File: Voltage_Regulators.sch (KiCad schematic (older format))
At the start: 28 parts, among them Q5 RTQ020N03, U1 LM2675_Adj, U2 LM2675_5V, U5 TLV2371_DBV

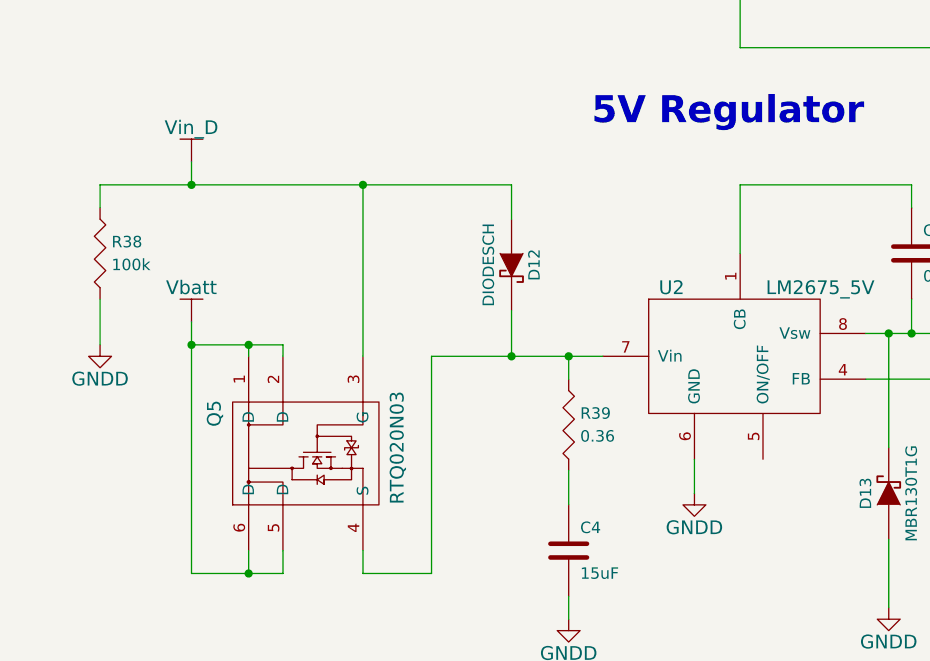
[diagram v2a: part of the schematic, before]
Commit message: Cleared all DRC errors.
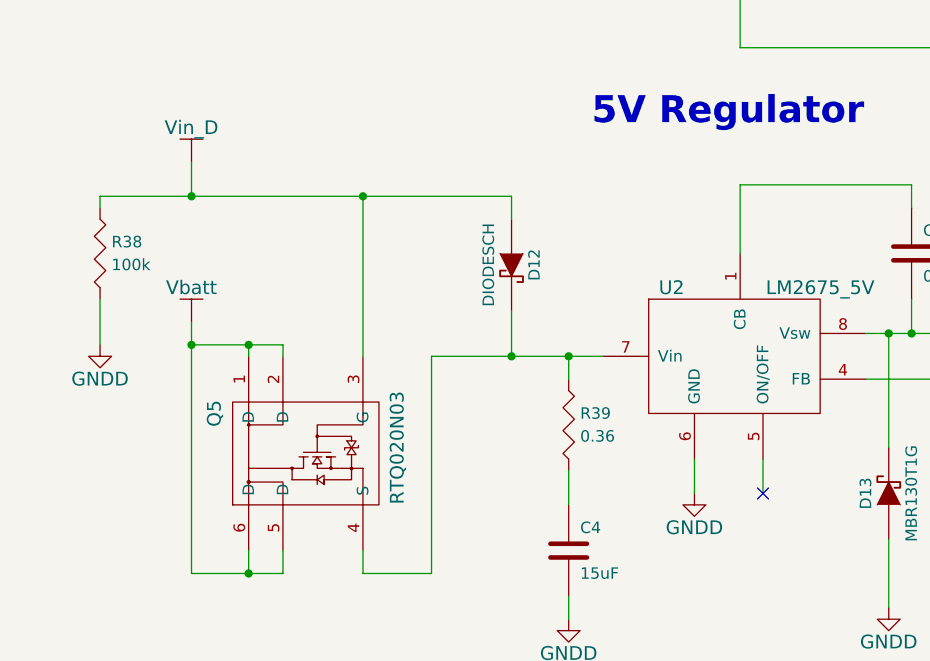
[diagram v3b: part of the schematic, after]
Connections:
- no-connect marks 0 -> 1
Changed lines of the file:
@@
 	5150 4900 5150 4700
 Connection ~ 5150 4900
-Wire Wire Line
-	5150 4150 5150 4300
-Wire Wire Line
-	3350 4150 5150 4150
-Wire Wire Line
-	4500 4150 4500 4900
-Connection ~ 4500 4150
-Wire Wire Line
-	3750 4150 3750 4050
 $Comp
 L Vbatt #PWR025
@@
 Wire Wire Line
 	3350 4650 3350 4850
-Wire Wire Line
-	3350 4250 3350 4150
-Connection ~ 3750 4150
 Text Notes 7600 1000 0    118  ~ 24
 8V Regulator
@@
 	1    0    0    -1
 $EndComp
+Wire Wire Line
+	4800 4900 4800 5850
+Wire Wire Line
+	4800 5850 4500 5850
+Wire Wire Line
+	4500 5850 4500 5750
+Wire Wire Line
+	4150 5850 4150 5750
+Wire Wire Line
+	3750 5850 4150 5850
+Wire Wire Line
+	4000 5850 4000 5750
+Connection ~ 4000 5850
+Wire Wire Line
+	3750 4850 4150 4850
+Wire Wire Line
+	4150 4850 4150 4900
+Connection ~ 3750 4850
+Wire Wire Line
+	4000 4850 4000 4900
+Connection ~ 4000 4850
+$Comp
+L TLV2371_DBV U5
+U 1 1 54FCB76E
+P 4650 2100
+F 0 "U5" H 4800 2250 60  0000 C CNN
+F 1 "TLV2371_DBV" H 4900 2350 60  0000 C CNN
+F 2 "KiCadFP:TSOT-6-MK06A_Handsoldering" H 4650 2100 60  0001 C CNN
+F 3 "" H 4650 2100 60  0000 C CNN
+	1    4650 2100
+	1    0    0    -1
+$EndComp
+Text Notes 7600 4050 0    60   ~ 0
+Changing SK12-13-F to  MBR130T1G
+Wire Wire Line
+	9400 2350 9400 2550
+Wire Wire Line
+	9400 2450 8700 2450
+Wire Wire Line
+	8700 2450 8700 2050
+Wire Wire Line
+	8700 2050 8350 2050
+Connection ~ 9400 2450
+$Comp
+L C C26
+U 1 1 54FF1862
+P 8500 5200
+F 0 "C26" H 8550 5300 50  0000 L CNN
+F 1 "10u" H 8550 5100 50  0000 L CNN
+F 2 "Capacitors_SMD:C_0603_HandSoldering" H 8538 5050 30  0001 C CNN
+F 3 "" H 8500 5200 60  0000 C CNN
+	1    8500 5200
+	1    0    0    -1
+$EndComp
+Wire Wire Line
+	8100 5550 9200 5550
+Wire Wire Line
+	9200 5550 9200 5400
+Connection ~ 8100 5550
+Wire Wire Line
+	8850 5400 8850 5550
+Connection ~ 8850 5550
+Wire Wire Line
+	8500 5550 8500 5400
+Connection ~ 8500 5550
+Wire Wire Line
+	8500 5000 8500 4900
+Wire Wire Line
+	8100 4900 9200 4900
+Connection ~ 8100 4900
+Wire Wire Line
+	8850 4900 8850 5000
+Connection ~ 8500 4900
+Wire Wire Line
+	9200 4900 9200 5000
+Connection ~ 8850 4900
+Wire Wire Line
+	10150 2450 10150 2550
+Wire Wire Line
+	9750 2550 10750 2550
+Connection ~ 9750 2550
+Wire Wire Line
+	10450 2550 10450 2450
+Connection ~ 10150 2550
+Wire Wire Line
+	10750 2550 10750 2450
+Connection ~ 10450 2550
+Wire Wire Line
+	9750 1900 10750 1900
+Wire Wire Line
+	10150 1900 10150 2050
+Connection ~ 9750 1900
+Wire Wire Line
+	10450 1900 10450 2050
+Connection ~ 10150 1900
+Wire Wire Line
+	10750 1900 10750 2050
+Connection ~ 10450 1900
+$Comp
+L C C27
+U 1 1 54FF22F3
+P 8850 5200
+F 0 "C27" H 8900 5300 50  0000 L CNN
+F 1 "10u" H 8900 5100 50  0000 L CNN
+F 2 "Capacitors_SMD:C_0603_HandSoldering" H 8888 5050 30  0001 C CNN
+F 3 "" H 8850 5200 60  0000 C CNN
+	1    8850 5200
+	1    0    0    -1
+$EndComp
+$Comp
+L C C28
+U 1 1 54FF2322
+P 9200 5200
+F 0 "C28" H 9250 5300 50  0000 L CNN
+F 1 "10u" H 9250 5100 50  0000 L CNN
+F 2 "Capacitors_SMD:C_0603_HandSoldering" H 9238 5050 30  0001 C CNN
+F 3 "" H 9200 5200 60  0000 C CNN
+	1    9200 5200
+	1    0    0    -1
+$EndComp
+$Comp
+L C C29
+U 1 1 54FF236E
+P 10150 2250
+F 0 "C29" H 10200 2350 50  0000 L CNN
+F 1 "10u" H 10200 2150 50  0000 L CNN
+F 2 "Capacitors_SMD:C_0603_HandSoldering" H 10188 2100 30  0001 C CNN
+F 3 "" H 10150 2250 60  0000 C CNN
+	1    10150 2250
+	1    0    0    -1
+$EndComp
+$Comp
+L C C30
+U 1 1 54FF23B3
+P 10450 2250
+F 0 "C30" H 10500 2350 50  0000 L CNN
+F 1 "10u" H 10500 2150 50  0000 L CNN
+F 2 "Capacitors_SMD:C_0603_HandSoldering" H 10488 2100 30  0001 C CNN
+F 3 "" H 10450 2250 60  0000 C CNN
+	1    10450 2250
+	1    0    0    -1
+$EndComp
+$Comp
+L C C31
+U 1 1 54FF23E9
+P 10750 2250
+F 0 "C31" H 10800 2350 50  0000 L CNN
+F 1 "10u" H 10800 2150 50  0000 L CNN
+F 2 "Capacitors_SMD:C_0603_HandSoldering" H 10788 2100 30  0001 C CNN
+F 3 "" H 10750 2250 60  0000 C CNN
+	1    10750 2250
+	1    0    0    -1
+$EndComp
+NoConn ~ 6250 5500
+Wire Wire Line
+	6250 5500 6250 5350
 $Comp
 L RTQ020N03 Q5
@@
 $EndComp
 Wire Wire Line
-	4500 4450 4500 4450
-Wire Wire Line
-	4800 4900 4800 5850
-Wire Wire Line
-	4800 5850 4500 5850
-Wire Wire Line
-	4500 5850 4500 5750
-Wire Wire Line
-	4150 5850 4150 5750
-Wire Wire Line
-	3750 5850 4150 5850
-Wire Wire Line
-	4000 5850 4000 5750
-Connection ~ 4000 5850
-Wire Wire Line
-	3750 4850 4150 4850
-Wire Wire Line
-	4150 4850 4150 4900
-Connection ~ 3750 4850
-Wire Wire Line
-	4000 4850 4000 4900
-Connection ~ 4000 4850
-$Comp
-L TLV2371_DBV U5
-U 1 1 54FCB76E
-P 4650 2100
-F 0 "U5" H 4800 2250 60  0000 C CNN
-F 1 "TLV2371_DBV" H 4900 2350 60  0000 C CNN
-F 2 "KiCadFP:TSOT-6-MK06A_Handsoldering" H 4650 2100 60  0001 C CNN
-F 3 "" H 4650 2100 60  0000 C CNN
-	1    4650 2100
-	1    0    0    -1
-$EndComp
-Text Notes 7600 4050 0    60   ~ 0
-Changing SK12-13-F to  MBR130T1G
-Wire Wire Line
-	9400 2350 9400 2550
-Wire Wire Line
-	9400 2450 8700 2450
-Wire Wire Line
-	8700 2450 8700 2050
-Wire Wire Line
-	8700 2050 8350 2050
-Connection ~ 9400 2450
-$Comp
-L C C26
-U 1 1 54FF1862
-P 8500 5200
-F 0 "C26" H 8550 5300 50  0000 L CNN
-F 1 "10u" H 8550 5100 50  0000 L CNN
-F 2 "Capacitors_SMD:C_0603_HandSoldering" H 8538 5050 30  0001 C CNN
-F 3 "" H 8500 5200 60  0000 C CNN
-	1    8500 5200
-	1    0    0    -1
-$EndComp
-Wire Wire Line
-	8100 5550 9200 5550
-Wire Wire Line
-	9200 5550 9200 5400
-Connection ~ 8100 5550
-Wire Wire Line
-	8850 5400 8850 5550
-Connection ~ 8850 5550
-Wire Wire Line
-	8500 5550 8500 5400
-Connection ~ 8500 5550
-Wire Wire Line
-	8500 5000 8500 4900
-Wire Wire Line
-	8100 4900 9200 4900
-Connection ~ 8100 4900
-Wire Wire Line
-	8850 4900 8850 5000
-Connection ~ 8500 4900
-Wire Wire Line
-	9200 4900 9200 5000
-Connection ~ 8850 4900
-Wire Wire Line
-	10150 2450 10150 2550
-Wire Wire Line
-	9750 2550 10750 2550
-Connection ~ 9750 2550
-Wire Wire Line
-	10450 2550 10450 2450
-Connection ~ 10150 2550
-Wire Wire Line
-	10750 2550 10750 2450
-Connection ~ 10450 2550
-Wire Wire Line
-	9750 1900 10750 1900
-Wire Wire Line
-	10150 1900 10150 2050
-Connection ~ 9750 1900
-Wire Wire Line
-	10450 1900 10450 2050
-Connection ~ 10150 1900
-Wire Wire Line
-	10750 1900 10750 2050
-Connection ~ 10450 1900
-$Comp
-L C C27
-U 1 1 54FF22F3
-P 8850 5200
-F 0 "C27" H 8900 5300 50  0000 L CNN
-F 1 "10u" H 8900 5100 50  0000 L CNN
-F 2 "Capacitors_SMD:C_0603_HandSoldering" H 8888 5050 30  0001 C CNN
-F 3 "" H 8850 5200 60  0000 C CNN
-	1    8850 5200
-	1    0    0    -1
-$EndComp
-$Comp
-L C C28
-U 1 1 54FF2322
-P 9200 5200
-F 0 "C28" H 9250 5300 50  0000 L CNN
-F 1 "10u" H 9250 5100 50  0000 L CNN
-F 2 "Capacitors_SMD:C_0603_HandSoldering" H 9238 5050 30  0001 C CNN
-F 3 "" H 9200 5200 60  0000 C CNN
-	1    9200 5200
-	1    0    0    -1
-$EndComp
-$Comp
-L C C29
-U 1 1 54FF236E
-P 10150 2250
-F 0 "C29" H 10200 2350 50  0000 L CNN
-F 1 "10u" H 10200 2150 50  0000 L CNN
-F 2 "Capacitors_SMD:C_0603_HandSoldering" H 10188 2100 30  0001 C CNN
-F 3 "" H 10150 2250 60  0000 C CNN
-	1    10150 2250
-	1    0    0    -1
-$EndComp
-$Comp
-L C C30
-U 1 1 54FF23B3
-P 10450 2250
-F 0 "C30" H 10500 2350 50  0000 L CNN
-F 1 "10u" H 10500 2150 50  0000 L CNN
-F 2 "Capacitors_SMD:C_0603_HandSoldering" H 10488 2100 30  0001 C CNN
-F 3 "" H 10450 2250 60  0000 C CNN
-	1    10450 2250
-	1    0    0    -1
-$EndComp
-$Comp
-L C C31
-U 1 1 54FF23E9
-P 10750 2250
-F 0 "C31" H 10800 2350 50  0000 L CNN
-F 1 "10u" H 10800 2150 50  0000 L CNN
-F 2 "Capacitors_SMD:C_0603_HandSoldering" H 10788 2100 30  0001 C CNN
-F 3 "" H 10750 2250 60  0000 C CNN
-	1    10750 2250
-	1    0    0    -1
-$EndComp
+	3350 4200 5150 4200
+Wire Wire Line
+	3350 4200 3350 4250
+Wire Wire Line
+	5150 4200 5150 4300
+Wire Wire Line
+	4500 4900 4500 4200
+Connection ~ 4500 4200
+Wire Wire Line
+	3750 4200 3750 4050
+Connection ~ 3750 4200
 $EndSCHEMATC
